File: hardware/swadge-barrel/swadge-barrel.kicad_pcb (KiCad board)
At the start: 2 copper layers, 70.4 x 89.6 mm, 48 parts, among them J1 USB_B_Micro, SW1 SW_SPDT, U1 AP1117-33, U2 ESP-13-WROOM-02D, U3 BUS_PCIexpress, U4 OLED_CONNECTOR, U5 QMA6981, U6 OLED_DISPLAY

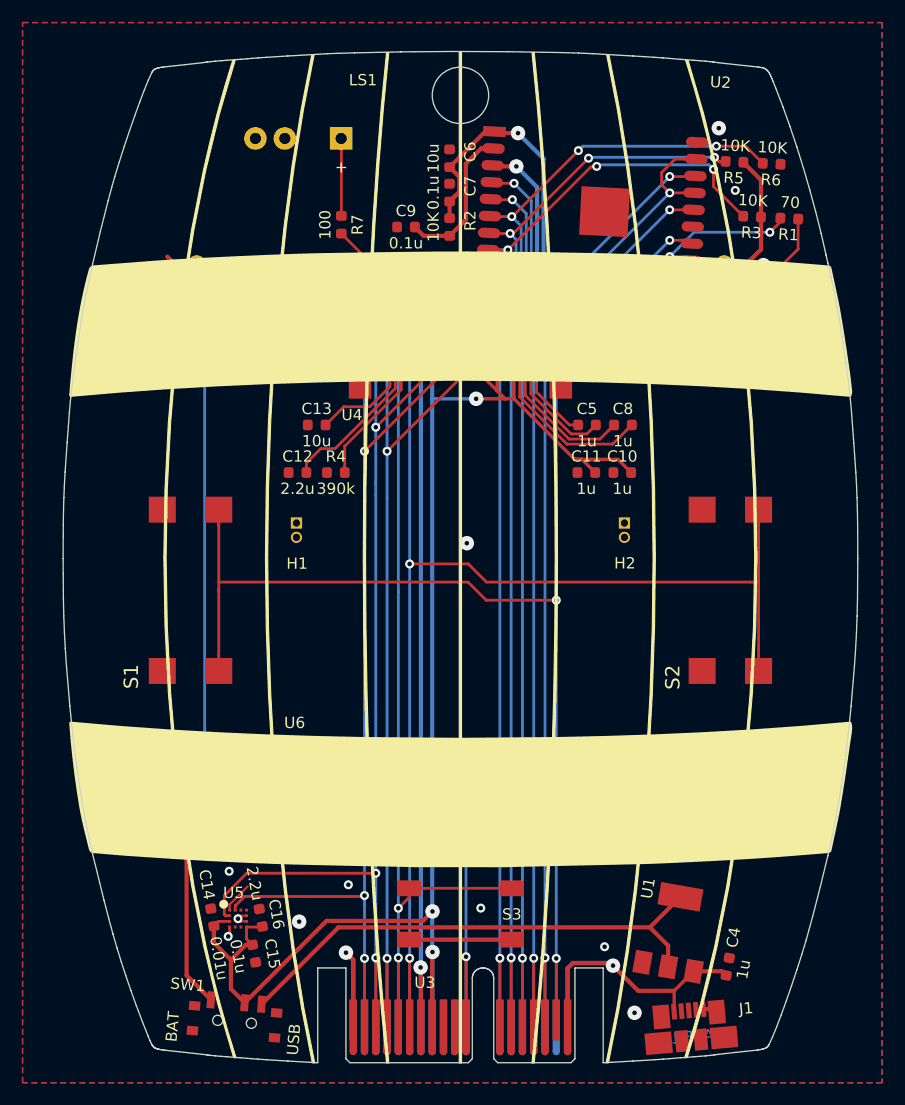
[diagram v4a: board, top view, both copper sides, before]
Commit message: Updated & added silkscreen  * Buttons  * PCIe connector  * Version  * Tilted MAGFEST logo  * Added note that USB is power-only  * Website text
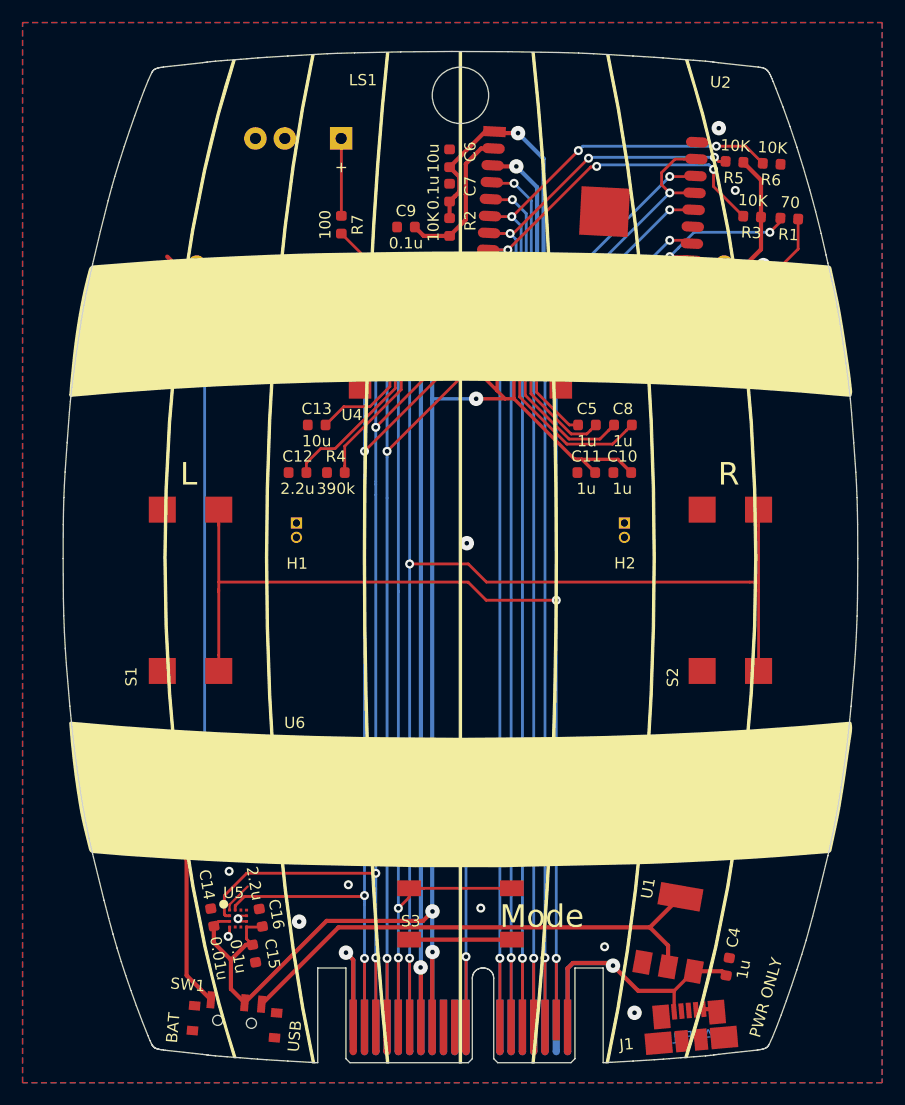
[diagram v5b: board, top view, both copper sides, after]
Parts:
- turned G*** to 190 degrees
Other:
- board text added: "3.3V"
- board text added: "5V"
- board text added: "BZR"
- board text added: "Barrel 1.0.4"
- board text added: "G14"
- board text added: "GND"
- board text added: "Instructions at http://swadge.com/super2020/"
- board text added: "L"
- board text added: "LED"
- board text added: "Mode"
- board text added: "PWR ONLY"
- board text added: "R"
- board text added: "REST"
- board text added: "RX"
- board text added: "S1"
- board text added: "S2"
- board text added: "S3"
- board text added: "SCL"
- board text added: "SDA"
- board text added: "Swadge 2020"
- board text added: "TOUT"
- board text added: "TX"
- board text added: "_RES"
- board text removed: "Barrel 1.0.3"
- board text removed: "http://swadge.com/super2020/"
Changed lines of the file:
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@@
   (general
     (thickness 1.6)
-    (drawings 377)
+    (drawings 398)
     (tracks 481)
     (zones 0)
@@
   (page A4)
   (layers
-    (0 F.Cu signal)
-    (31 B.Cu signal hide)
-    (32 B.Adhes user)
-    (33 F.Adhes user)
+    (0 F.Cu signal hide)
+    (31 B.Cu signal)
+    (32 B.Adhes user hide)
+    (33 F.Adhes user hide)
     (34 B.Paste user)
-    (35 F.Paste user)
+    (35 F.Paste user hide)
     (36 B.SilkS user)
-    (37 F.SilkS user)
+    (37 F.SilkS user hide)
     (38 B.Mask user)
-    (39 F.Mask user)
-    (40 Dwgs.User user)
-    (41 Cmts.User user)
-    (42 Eco1.User user)
-    (43 Eco2.User user)
+    (39 F.Mask user hide)
+    (40 Dwgs.User user hide)
+    (41 Cmts.User user hide)
+    (42 Eco1.User user hide)
+    (43 Eco2.User user hide)
     (44 Edge.Cuts user)
-    (45 Margin user)
+    (45 Margin user hide)
     (46 B.CrtYd user)
-    (47 F.CrtYd user)
+    (47 F.CrtYd user hide)
     (48 B.Fab user)
-    (49 F.Fab user)
+    (49 F.Fab user hide)
   )
   (setup
@@
   )
   (module Swadge_Parts:mag-logo-outline (layer B.Cu)
-    (at 154.1526 64.7446 180)
-    (fp_text reference G*** (at 0 0) (layer B.SilkS) hide
+    (at 154.1526 64.7446 190)
+    (fp_text reference G*** (at 0 0 10) (layer B.SilkS) hide
       (effects (font (size 1.524 1.524) (thickness 0.3)) (justify mirror))
     )
-    (fp_text value LOGO (at 0.75 0) (layer B.SilkS) hide
+    (fp_text value LOGO (at 0.75 0 10) (layer B.SilkS) hide
       (effects (font (size 1.524 1.524) (thickness 0.3)) (justify mirror))
     )
@@
     (tags "Micro B USB SMD")
     (attr smd)
-    (fp_text reference J1 (at 5.081807 -1.198653 185) (layer F.SilkS)
+    (fp_text reference J1 (at -5.752382 1.05205 185) (layer F.SilkS)
       (effects (font (size 1 1) (thickness 0.15)))
     )
@@
     (at 145.4968 129.8194)
     (attr smd)
-    (fp_text reference S3 (at 4.5532 0.0306) (layer F.SilkS)
+    (fp_text reference S3 (at -4.40996 0.62992) (layer F.SilkS)
       (effects (font (size 1 1) (thickness 0.15)))
     )
@@
     (attr smd)
     (fp_text reference S2 (at -8.84 -5.102571 90) (layer F.SilkS)
-      (effects (font (size 1.27 1.27) (thickness 0.254)))
+      (effects (font (size 1 1) (thickness 0.15)))
     )
     (fp_text value B3FS-4002P (at -1.143 7.366 90) (layer F.Fab) hide
@@
     (attr smd)
     (fp_text reference S1 (at -8.78 -5.251 90) (layer F.SilkS)
-      (effects (font (size 1.27 1.27) (thickness 0.254)))
+      (effects (font (size 1 1) (thickness 0.15)))
     )
     (fp_text value B3FS-4002P (at -1.143 7.366 90) (layer F.Fab) hide
@@
     (tags "PCIexpress Bus Edge Connector")
     (attr virtual)
-    (fp_text reference U3 (at 6.35 -3.31) (layer F.SilkS)
+    (fp_text reference U3 (at 6.35 -3.31) (layer F.SilkS) hide
       (effects (font (size 1 1) (thickness 0.15)))
     )
@@
     )
   )
-  (gr_text USB (at 130.72872 140.94968 85) (layer F.SilkS)
+  (gr_text "PWR ONLY" (at 172.57776 137.22604 74) (layer F.SilkS)
+    (effects (font (size 1 1) (thickness 0.15)))
+  )
+  (gr_text Mode (at 152.71496 130.03276) (layer F.SilkS)
+    (effects (font (size 2 2) (thickness 0.3)))
+  )
+  (gr_text R (at 169.27576 90.8304) (layer F.SilkS)
+    (effects (font (size 2 2) (thickness 0.3)))
+  )
+  (gr_text L (at 121.40692 90.8304) (layer F.SilkS)
+    (effects (font (size 2 2) (thickness 0.3)))
+  )
+  (gr_text GND (at 135.98144 136.2964 270) (layer B.SilkS)
+    (effects (font (size 0.5 0.5) (thickness 0.075)) (justify mirror))
+  )
+  (gr_text SCL (at 136.98728 136.2964 270) (layer B.SilkS)
+    (effects (font (size 0.5 0.5) (thickness 0.075)) (justify mirror))
+  )
+  (gr_text SDA (at 137.99312 136.2964 270) (layer B.SilkS)
+    (effects (font (size 0.5 0.5) (thickness 0.075)) (justify mirror))
+  )
+  (gr_text _RES (at 138.98372 136.2964 270) (layer B.SilkS)
+    (effects (font (size 0.5 0.5) (thickness 0.075)) (justify mirror))
+  )
+  (gr_text S2 (at 139.98956 136.2964 270) (layer B.SilkS)
+    (effects (font (size 0.5 0.5) (thickness 0.075)) (justify mirror))
+  )
+  (gr_text S1 (at 141.00048 136.2964 270) (layer B.SilkS)
+    (effects (font (size 0.5 0.5) (thickness 0.075)) (justify mirror))
+  )
+  (gr_text G14 (at 142.00124 136.2964 270) (layer B.SilkS)
+    (effects (font (size 0.5 0.5) (thickness 0.075)) (justify mirror))
+  )
+  (gr_text 3.3V (at 143.00708 136.2964 270) (layer B.SilkS)
+    (effects (font (size 0.5 0.5) (thickness 0.075)) (justify mirror))
+  )
+  (gr_text LED (at 145.98396 136.2964 270) (layer B.SilkS)
+    (effects (font (size 0.5 0.5) (thickness 0.075)) (justify mirror))
+  )
+  (gr_text TOUT (at 148.99132 136.2964 270) (layer B.SilkS)
+    (effects (font (size 0.5 0.5) (thickness 0.075)) (justify mirror))
+  )
+  (gr_text REST (at 149.987 136.2964 270) (layer B.SilkS)
+    (effects (font (size 0.5 0.5) (thickness 0.075)) (justify mirror))
+  )
+  (gr_text BZR (at 150.99284 136.2964 270) (layer B.SilkS)
+    (effects (font (size 0.5 0.5) (thickness 0.075)) (justify mirror))
+  )
+  (gr_text TX (at 151.9936 136.2964 270) (layer B.SilkS)
+    (effects (font (size 0.5 0.5) (thickness 0.075)) (justify mirror))
+  )
+  (gr_text RX (at 152.9842 136.2964 270) (layer B.SilkS)
+    (effects (font (size 0.5 0.5) (thickness 0.075)) (justify mirror))
+  )
+  (gr_text S3 (at 154.01036 136.2964 270) (layer B.SilkS)
+    (effects (font (size 0.5 0.5) (thickness 0.075)) (justify mirror))
+  )
+  (gr_text 5V (at 155.0162 136.2964 270) (layer B.SilkS)
+    (effects (font (size 0.5 0.5) (thickness 0.075)) (justify mirror))
+  )
+  (gr_text "Barrel 1.0.4" (at 125.5522 64.14516) (layer B.SilkS)
+    (effects (font (size 2 2) (thickness 0.3)) (justify mirror))
+  )
+  (gr_text USB (at 130.81 140.64996 85) (layer F.SilkS)
     (effects (font (size 1 1) (thickness 0.15)))
   )
-  (gr_text BAT (at 119.97944 139.80668 85) (layer F.SilkS)
+  (gr_text BAT (at 120.02008 139.9032 85) (layer F.SilkS)
     (effects (font (size 1 1) (thickness 0.15)))
   )
@@
     (effects (font (size 1 1) (thickness 0.15)) (justify mirror))
   )
-  (gr_text http://swadge.com/super2020/ (at 145.5166 130.3528) (layer B.SilkS)
-    (effects (font (size 2.4 2.4) (thickness 0.3)) (justify mirror))
+  (gr_text "Instructions at http://swadge.com/super2020/" (at 145.5166 130.3528) (layer B.SilkS)
+    (effects (font (size 1.6 1.6) (thickness 0.275)) (justify mirror))
   )
   (gr_poly (pts (xy 151.835884 53.442005) (xy 152.304799 58.253345) (xy 152.716938 63.355966) (xy 153.070529 68.716613) (xy 153.363802 74.302033) (xy 153.594985 80.078971) (xy 153.762308 86.014172) (xy 153.864001 92.074382) (xy 153.898292 98.226347) (xy 153.863941 104.382621) (xy 153.762073 110.446949) (xy 153.594472 116.386018) (xy 153.362917 122.166516) (xy 153.069189 127.755129) (xy 152.715071 133.118544) (xy 152.302343 138.223448) (xy 151.832786 143.036528) (xy 152.033805 143.036528) (xy 152.503252 138.22122) (xy 152.915833 133.115002) (xy 153.269782 127.751049) (xy 153.563335 122.162535) (xy 153.794726 116.382634) (xy 153.962191 110.444519) (xy 154.063965 104.381366) (xy 154.098281 98.226347) (xy 154.064017 92.076122) (xy 153.962398 86.017523) (xy 153.795186 80.083666) (xy 153.564143 74.307669) (xy 153.271032 68.722646) (xy 152.917614 63.361715) (xy 152.505652 58.25799) (xy 152.036907 53.444589) (xy 151.835884 53.442005)) (layer F.SilkS) (width 0.099999))
@@
   (gr_poly (pts (xy 139.146221 53.453374) (xy 138.944683 53.457508) (xy 138.476254 58.27004) (xy 138.064585 63.372615) (xy 137.711432 68.732148) (xy 137.418549 74.31556) (xy 137.187695 80.089768) (xy 137.020624 86.021689) (xy 136.919094 92.078243) (xy 136.884861 98.226347) (xy 136.919177 104.381366) (xy 137.02095 110.444519) (xy 137.188414 116.382634) (xy 137.419805 122.162535) (xy 137.713358 127.751049) (xy 138.067307 133.115002) (xy 138.479887 138.22122) (xy 138.949335 143.036528) (xy 139.150356 143.036528) (xy 138.6808 138.223448) (xy 138.268071 133.118543) (xy 137.913953 127.755126) (xy 137.620225 122.166512) (xy 137.38867 116.386013) (xy 137.221067 110.446944) (xy 137.1192 104.382617) (xy 137.084848 98.226347) (xy 137.119126 92.076249) (xy 137.220778 86.017839) (xy 137.38803 80.084342) (xy 137.619108 74.308981) (xy 137.91224 68.72498) (xy 138.265652 63.365563) (xy 138.67757 58.263953) (xy 139.146221 53.453374)) (layer F.SilkS) (width 0.099999))
   (gr_poly (pts (xy 125.53 54.12) (xy 125.313993 54.136536) (xy 124.597446 56.483852) (xy 123.922624 58.903932) (xy 123.29015 61.392848) (xy 122.700644 63.946674) (xy 121.653024 69.23335) (xy 120.784734 74.732551) (xy 120.100745 80.412863) (xy 119.606027 86.242874) (xy 119.305551 92.191172) (xy 119.204288 98.226347) (xy 119.306883 104.300657) (xy 119.611286 110.286704) (xy 120.112422 116.152471) (xy 120.805217 121.865938) (xy 121.684597 127.395088) (xy 122.745488 132.707903) (xy 123.982816 137.772365) (xy 125.391507 142.556456) (xy 125.606998 142.572996) (xy 124.880258 140.220462) (xy 124.195694 137.793166) (xy 123.553957 135.295151) (xy 122.955696 132.730464) (xy 121.892203 127.417257) (xy 121.010414 121.885906) (xy 120.315527 116.168776) (xy 119.812743 110.29823) (xy 119.50726 104.306632) (xy 119.404276 98.226347) (xy 119.505949 92.185228) (xy 119.807562 86.231435) (xy 120.304009 80.396709) (xy 120.990182 74.712791) (xy 121.860975 69.21142) (xy 122.91128 63.924338) (xy 124.135991 58.883284) (xy 125.53 54.12)) (layer F.SilkS) (width 0.099999))
-  (gr_text "Barrel 1.0.3" (at 128.625 57.325) (layer B.SilkS)
+  (gr_text "Swadge 2020" (at 128.625 57.325) (layer B.SilkS)
     (effects (font (size 2 2) (thickness 0.3)) (justify mirror))
   )

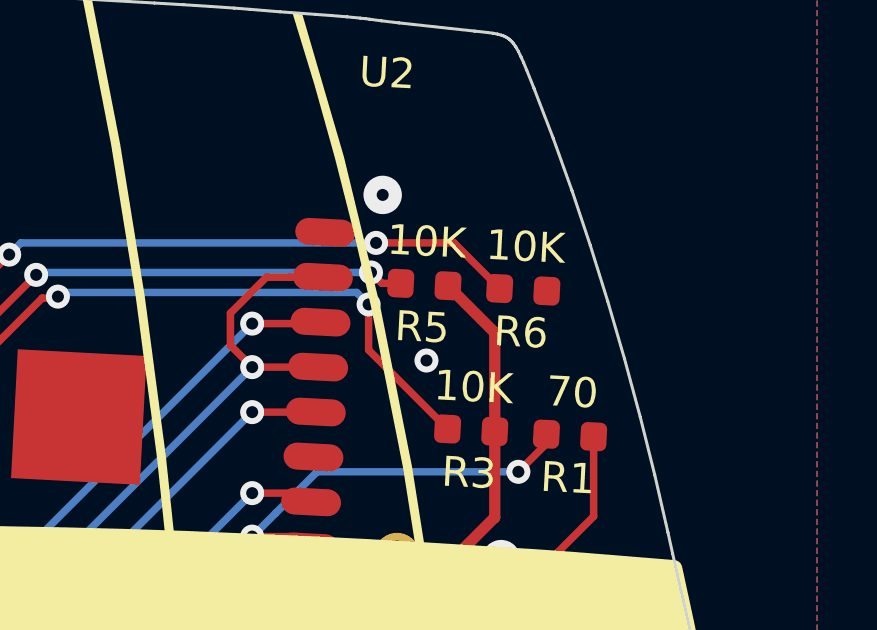
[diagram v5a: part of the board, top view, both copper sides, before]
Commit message: Changed I2C pullups to 1K Updated digikey part numbers on BOM
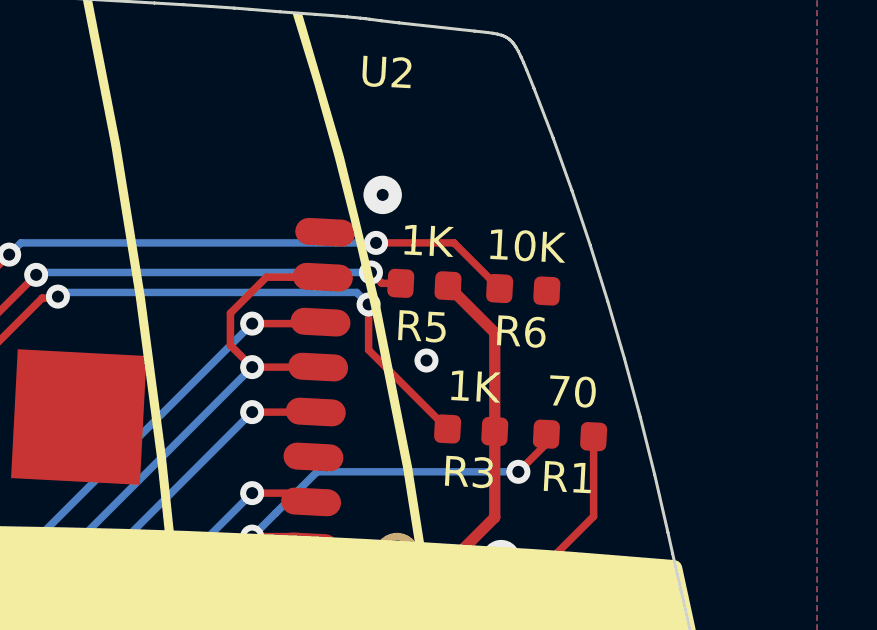
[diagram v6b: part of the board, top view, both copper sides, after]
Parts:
- R3, R5: value 10K -> 1K
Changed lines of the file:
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@@
   (page A4)
   (layers
-    (0 F.Cu signal hide)
+    (0 F.Cu signal)
     (31 B.Cu signal)
-    (32 B.Adhes user hide)
-    (33 F.Adhes user hide)
+    (32 B.Adhes user)
+    (33 F.Adhes user)
     (34 B.Paste user)
-    (35 F.Paste user hide)
+    (35 F.Paste user)
     (36 B.SilkS user)
-    (37 F.SilkS user hide)
+    (37 F.SilkS user)
     (38 B.Mask user)
-    (39 F.Mask user hide)
-    (40 Dwgs.User user hide)
-    (41 Cmts.User user hide)
-    (42 Eco1.User user hide)
-    (43 Eco2.User user hide)
+    (39 F.Mask user)
+    (40 Dwgs.User user)
+    (41 Cmts.User user)
+    (42 Eco1.User user)
+    (43 Eco2.User user)
     (44 Edge.Cuts user)
-    (45 Margin user hide)
+    (45 Margin user)
     (46 B.CrtYd user)
-    (47 F.CrtYd user hide)
+    (47 F.CrtYd user)
     (48 B.Fab user)
-    (49 F.Fab user hide)
+    (49 F.Fab user)
   )
   (setup
@@
       (effects (font (size 1 1) (thickness 0.15)))
     )
-    (fp_text value 10K (at 0 1.43 177) (layer F.SilkS)
+    (fp_text value 1K (at 0 1.43 177) (layer F.SilkS)
       (effects (font (size 1 1) (thickness 0.15)))
     )
@@
       (effects (font (size 1 1) (thickness 0.15)))
     )
-    (fp_text value 10K (at 0 1.43 177) (layer F.SilkS)
+    (fp_text value 1K (at 0 1.43 177) (layer F.SilkS)
       (effects (font (size 1 1) (thickness 0.15)))
     )
